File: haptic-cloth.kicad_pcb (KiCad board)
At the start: 2 copper layers, 24 x 16 mm, 16 parts, among them J1 Conn_01x03, J2 Conn_01x03, J3 Prog, M1 Motor_DC, Q1 BSS138, U1 PFS172-SO8

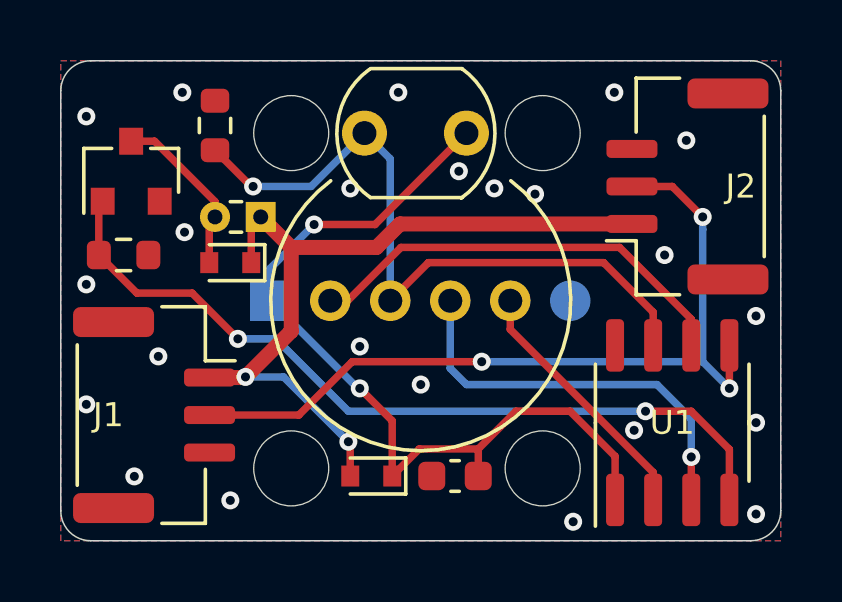
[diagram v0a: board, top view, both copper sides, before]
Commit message: Shift motor connector further away
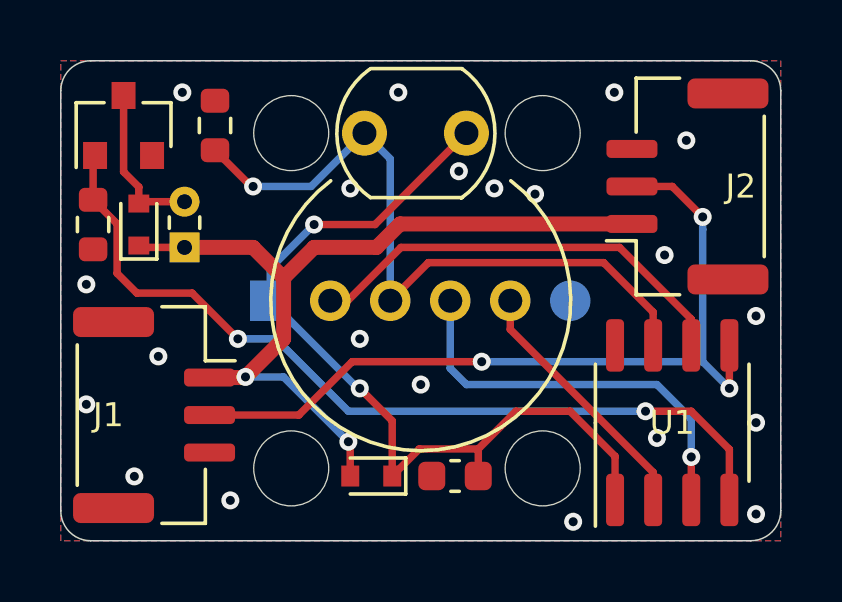
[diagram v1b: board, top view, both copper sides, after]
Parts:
- moved D1 3.30 mm to (179.8, 101.1), turned to 90 degrees
- moved M1 1.80 mm to (181.3, 101.1), turned to 90 degrees
- moved Q1 1.55 mm to (179.3, 97.8)
- moved R3 1.44 mm to (178.2, 101.1), turned to 270 degrees
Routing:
- net VCC: track 26.2 -> 28.2 mm
- net /PB7: track 27.2 -> 28.8 mm
- net GND: vias 23 -> 21

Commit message: Fix 3D models
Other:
- board text added: "Haptic Cloth Rev 1"
- board text added: "Nov 2021"
- board text removed: "Haptic Cloth Rev 1 Nov 2021"
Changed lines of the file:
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@@
-(kicad_pcb (version 20171130) (host pcbnew "(5.1.7)-1")
+(kicad_pcb (version 20171130) (host pcbnew "(5.1.8)-1")
   (general
     (thickness 1.6)
-    (drawings 16)
+    (drawings 17)
     (tracks 118)
     (zones 0)
@@
     (pad 1 smd rect (at 0 0 270) (size 1.35 1.35) (layers B.Cu B.Paste B.Mask)
       (net 8 /MCU_VCC))
-    (model ${KISYS3DMOD}/Connector_PinHeader_2.00mm.3dshapes/PinHeader_1x06_P2.00mm_Vertical.wrl
-      (at (xyz 0 0 0))
-      (scale (xyz 1 1 1))
-      (rotate (xyz 0 0 0))
-    )
   )
   (module Resistor_SMD:R_0603_1608Metric (layer F.Cu)
@@
       (rotate (xyz 0 0 0))
     )
+    (model ${KISYS3DMOD}/Package_SO.3dshapes/HTSOP-8-1EP_3.9x4.9mm_Pitch1.27mm.wrl
+      (at (xyz 0 0 0))
+      (scale (xyz 1 1 1))
+      (rotate (xyz 0 0 0))
+    )
   )
   (module haptic-cloth:Motor (layer F.Cu)
@@
     (pad 1 thru_hole rect (at -0.762 0 180) (size 1 1) (drill 0.5) (layers *.Cu *.Mask)
       (net 2 VCC))
+    (model "${KIPRJMOD}/1030 Vibration Motor v1.step"
+      (offset (xyz -2.45 -8 0.1))
+      (scale (xyz 1 1 1))
+      (rotate (xyz -90 0 0))
+    )
   )
   (module "haptic-cloth:Mounting Hole" (layer F.Cu)
@@
       (net 8 /MCU_VCC))
     (model ${KISYS3DMOD}/OptoDevice.3dshapes/R_LDR_5.1x4.3mm_P3.4mm_Vertical.wrl
-      (at (xyz 0 0 0))
+      (offset (xyz 0 0 1))
       (scale (xyz 1 1 1))
       (rotate (xyz 0 0 0))
@@
     )
   )
-  (gr_text "Haptic Cloth Rev 1\nNov 2021" (at 180.016 103.6 90) (layer B.SilkS)
+  (gr_text "Nov 2021" (at 181.286 105.886 90) (layer B.SilkS)
+    (effects (font (size 0.8 0.8) (thickness 0.15)) (justify mirror))
+  )
+  (gr_text "Haptic Cloth Rev 1" (at 179.254 103.6 90) (layer B.SilkS)
     (effects (font (size 1 1) (thickness 0.15)) (justify mirror))
   )
